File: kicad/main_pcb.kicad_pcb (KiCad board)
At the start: 2 copper layers, 147.4 x 112.7 mm, 81 parts

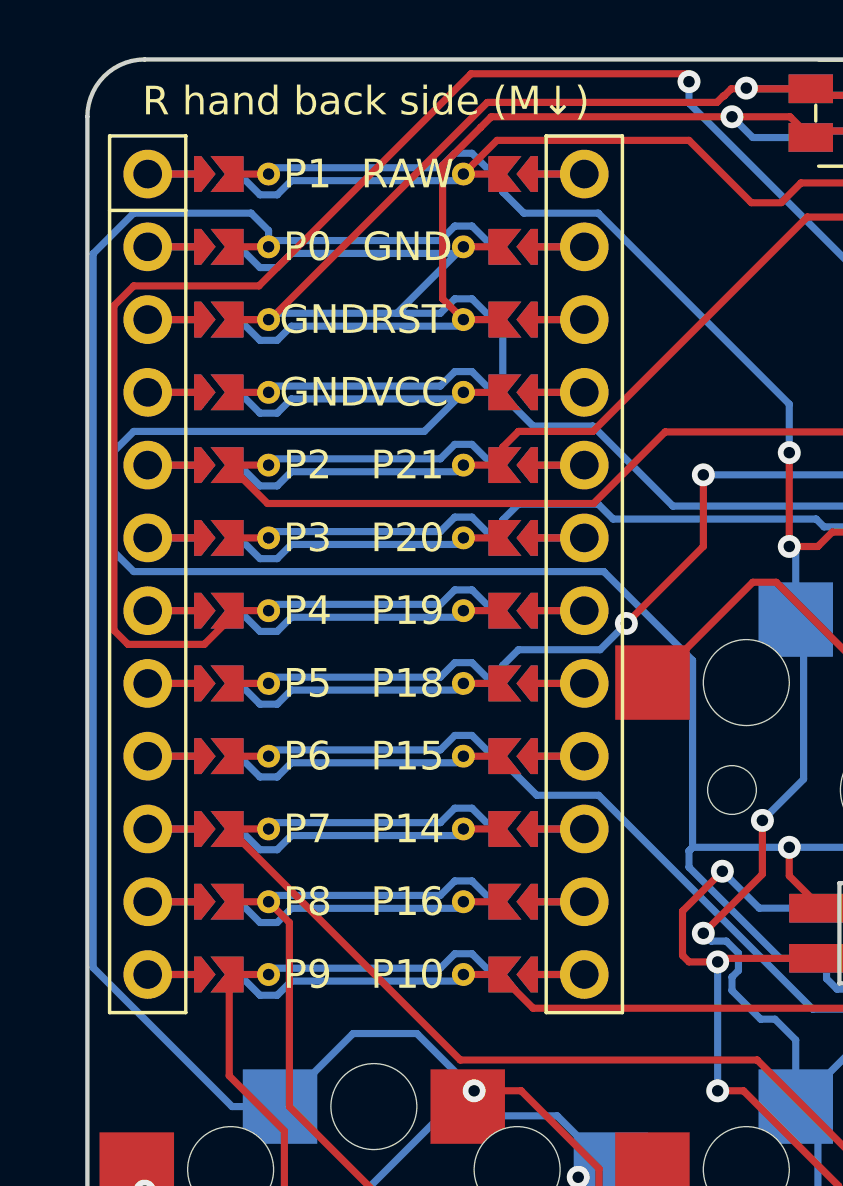
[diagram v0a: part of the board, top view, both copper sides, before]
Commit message: Add top plate
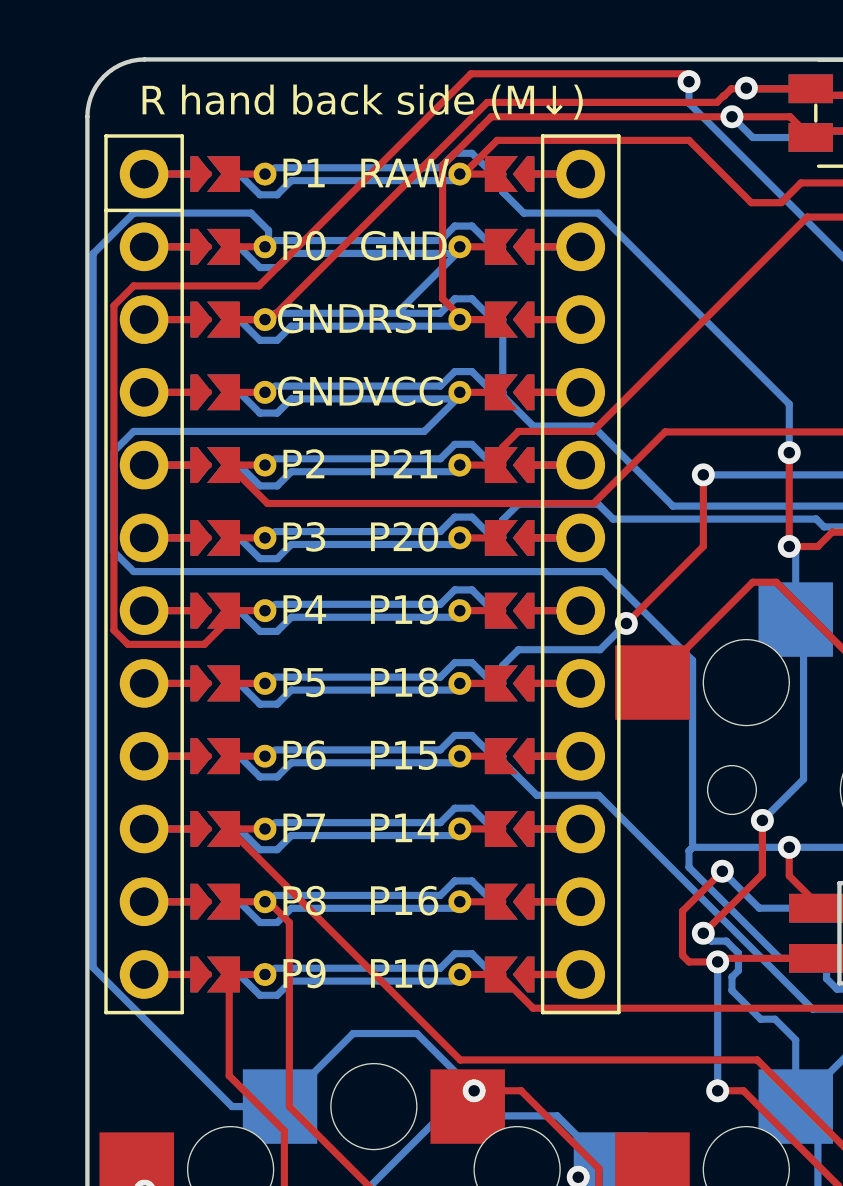
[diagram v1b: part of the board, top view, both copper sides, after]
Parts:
- moved MCU1 0.12 mm to (81.6, 90.2)
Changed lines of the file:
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@@
 			(outputformat 1)
 			(mirror no)
-			(drillshape 1)
+			(drillshape 0)
 			(scaleselection 1)
-			(outputdirectory "")
+			(outputdirectory "gerber")
 		)
 	)
@@
 	(footprint "ceoloide:mcu_supermini_nrf52840"
 		(layer "F.Cu")
-		(at 81.725 90.2)
+		(at 81.6 90.2)
 		(property "Reference" "MCU1"
 			(at 0 -15 0)
